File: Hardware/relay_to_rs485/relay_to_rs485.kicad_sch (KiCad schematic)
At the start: 38 parts, among them J1 Relay Inputs A to E connected, J2 RS485 Output Screw Terminal, J3 Screw_Terminal_InputGrounds, J4 Jack-DC, J5 UART OUT, Q1 IRLML6401, U1 ESP32-S3-WROOM-1, U2 MAX485E, U3 SMX1117MP-3.3

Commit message: Minor rotation of J2 labelling on schematic
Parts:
- added TP16, TP17: ~, TestPoint:TestPoint_Pad_1.5x1.5mm, symbol Connector:TestPoint_Probe
- renumbered TP1 to TP1_A1, TP2 to TP2_B1, TP3 to TP3_C1, TP4 to TP4_D1, TP5 to TP5_E1, TP6 to TP6_F1, TP7 to TP7_G1, TP8 to TP8_H1
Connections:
- net RX: now also TP17.1
- net TX: now also TP16.1
- net at U1.35 (IO42), U2.1 (RO): now also TP11.1
- net at U1.30 (IO37), U2.2 (~{RE}), U2.3 (DE): no longer TP11.1

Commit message: various edits
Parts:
- added R4, R5: 680R, Resistor_SMD:R_0805_2012Metric_Pad1.20x1.40mm_HandSolder, symbol Device:R
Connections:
- net +3V3: now also R4.1
- net A: now also R4.2
- net B: now also R5.1
- net GND: now also R5.2

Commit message: Changed decoupling resistor values from 100uF to 1uF
Too high capacitance
Also changed silkscreen for R1 to make clear terminating resistor
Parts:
- C2, C4, C7: value 100uF -> 1uF
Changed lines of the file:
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@@
 			)
 		)
-		(property "Value" "100uF"
+		(property "Value" "1uF"
 			(at 214.122 77.724 90)
 			(effects
@@
 			)
 		)
-		(property "Value" "100uF"
+		(property "Value" "1uF"
 			(at 141.732 68.834 90)
 			(effects
@@
 		)
 		(property "Value" "Jack-DC"
-			(at 19.05 29.2101 0)
+			(at 19.05 35.306 90)
 			(effects
 				(font
@@
 			)
 		)
-		(property "Value" "100uF"
+		(property "Value" "1uF"
 			(at 61.214 43.434 90)
 			(effects

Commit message: Change of DC polarity marking on PCB
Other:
- title: (none) -> Relay to RS485 Module
- moved on the sheet: R1
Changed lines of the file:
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@@
 	(generator_version "8.0")
 	(paper "A4")
+	(title_block
+		(title "Relay to RS485 Module")
+		(date "2024-09-09")
+	)
 	(junction
 		(at 60.96 35.56)
@@
 	)
 	(junction
+		(at 238.76 106.68)
+		(diameter 0)
+		(color 0 0 0 0)
+	)
+	(junction
 		(at 218.44 86.36)
 		(diameter 0)
@@
 	)
 	(junction
+		(at 238.76 101.6)
+		(diameter 0)
+		(color 0 0 0 0)
+	)
+	(junction
 		(at 251.46 101.6)
 		(diameter 0)
@@
 	(wire
 		(pts
-			(xy 232.41 101.6) (xy 245.11 101.6)
+			(xy 232.41 101.6) (xy 238.76 101.6)
 		)
 		(stroke
@@
 	(wire
 		(pts
-			(xy 232.41 106.68) (xy 250.19 106.68)
+			(xy 232.41 106.68) (xy 238.76 106.68)
 		)
 		(stroke
@@
 	(wire
 		(pts
+			(xy 238.76 106.68) (xy 250.19 106.68)
+		)
+		(stroke
+			(width 0)
+			(type default)
+		)
+	)
+	(wire
+		(pts
 			(xy 53.34 35.56) (xy 48.26 35.56)
 		)
@@
 		(pts
 			(xy 250.19 106.68) (xy 250.19 110.49)
+		)
+		(stroke
+			(width 0)
+			(type default)
+		)
+	)
+	(wire
+		(pts
+			(xy 238.76 101.6) (xy 245.11 101.6)
 		)
 		(stroke
@@
 	(symbol
 		(lib_id "Device:R_Small")
-		(at 232.41 104.14 0)
+		(at 238.76 104.14 0)
 		(unit 1)
 		(exclude_from_sim no)
@@
 		(fields_autoplaced yes)
 		(property "Reference" "R1"
-			(at 234.95 102.8699 0)
+			(at 241.3 102.8699 0)
 			(effects
 				(font
@@
 		)
 		(property "Value" "100R"
-			(at 234.95 105.4099 0)
+			(at 241.3 105.4099 0)
 			(effects
 				(font
@@
 		)
 		(property "Footprint" "Resistor_SMD:R_0805_2012Metric_Pad1.20x1.40mm_HandSolder"
-			(at 232.41 104.14 0)
+			(at 238.76 104.14 0)
 			(effects
 				(font
@@
 		)
 		(property "Datasheet" "~"
-			(at 232.41 104.14 0)
+			(at 238.76 104.14 0)
 			(effects
 				(font
@@
 		)
 		(property "Description" "Resistor, small symbol"
-			(at 232.41 104.14 0)
-			(effects
-				(font
+			(at 238.76 104.14 0)
+			(effects
+				(font

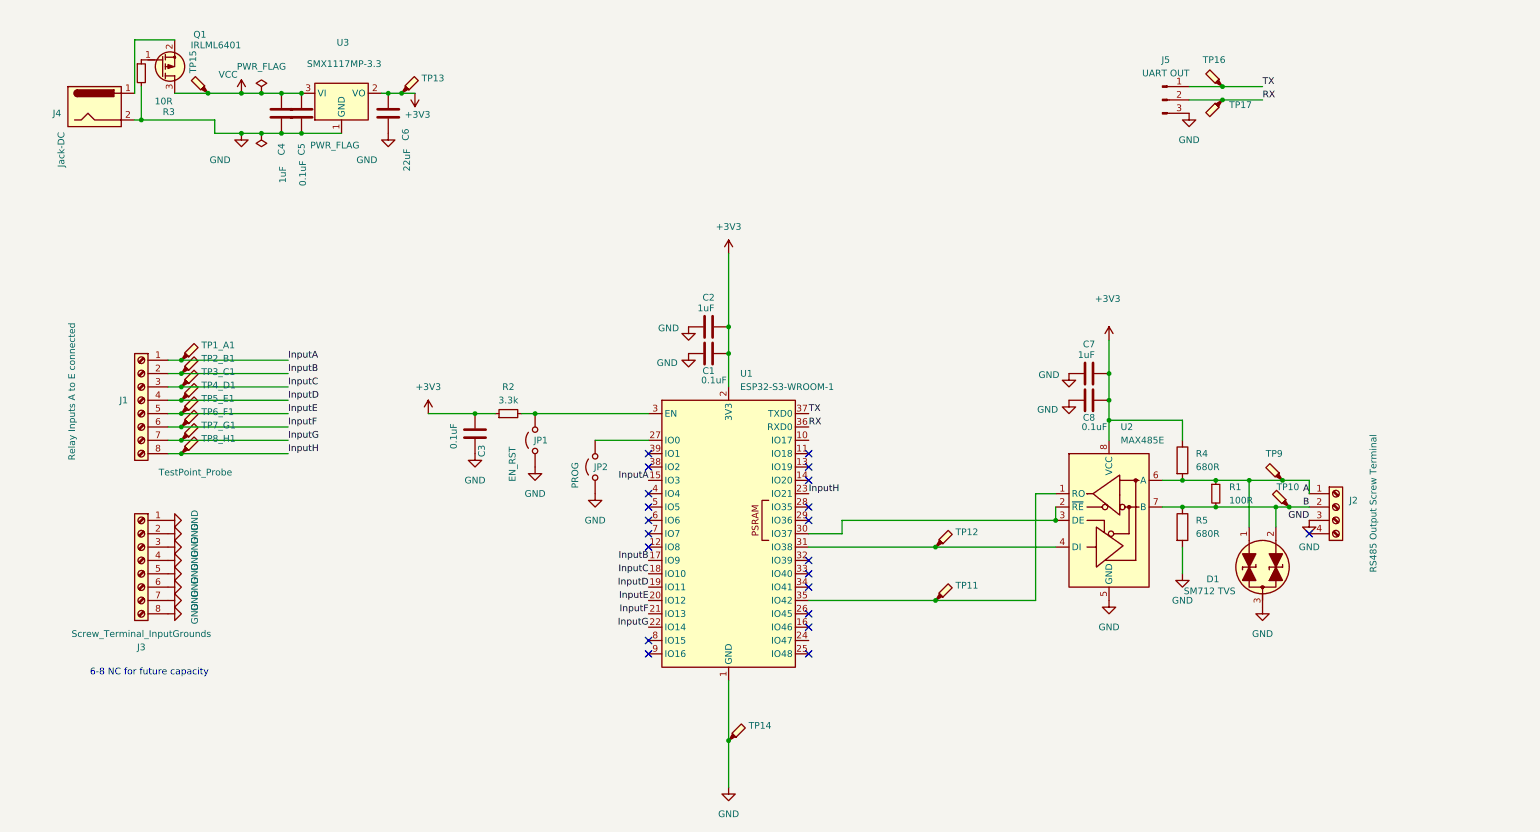
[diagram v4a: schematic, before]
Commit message: Revision B of Board (2.0.0)
Add:
1. LC filter on 3.3V input
2. Change trace widths to 20mil for 3.3V and 25mil for VCC as per Espressif documentation
3. Add-in 470R UART Tx resistors to suppress 80MHz harmonics
4. Rerouting of components around MAX3485 chip
5. Change value of R2 EN pullup resistor to 4.7k
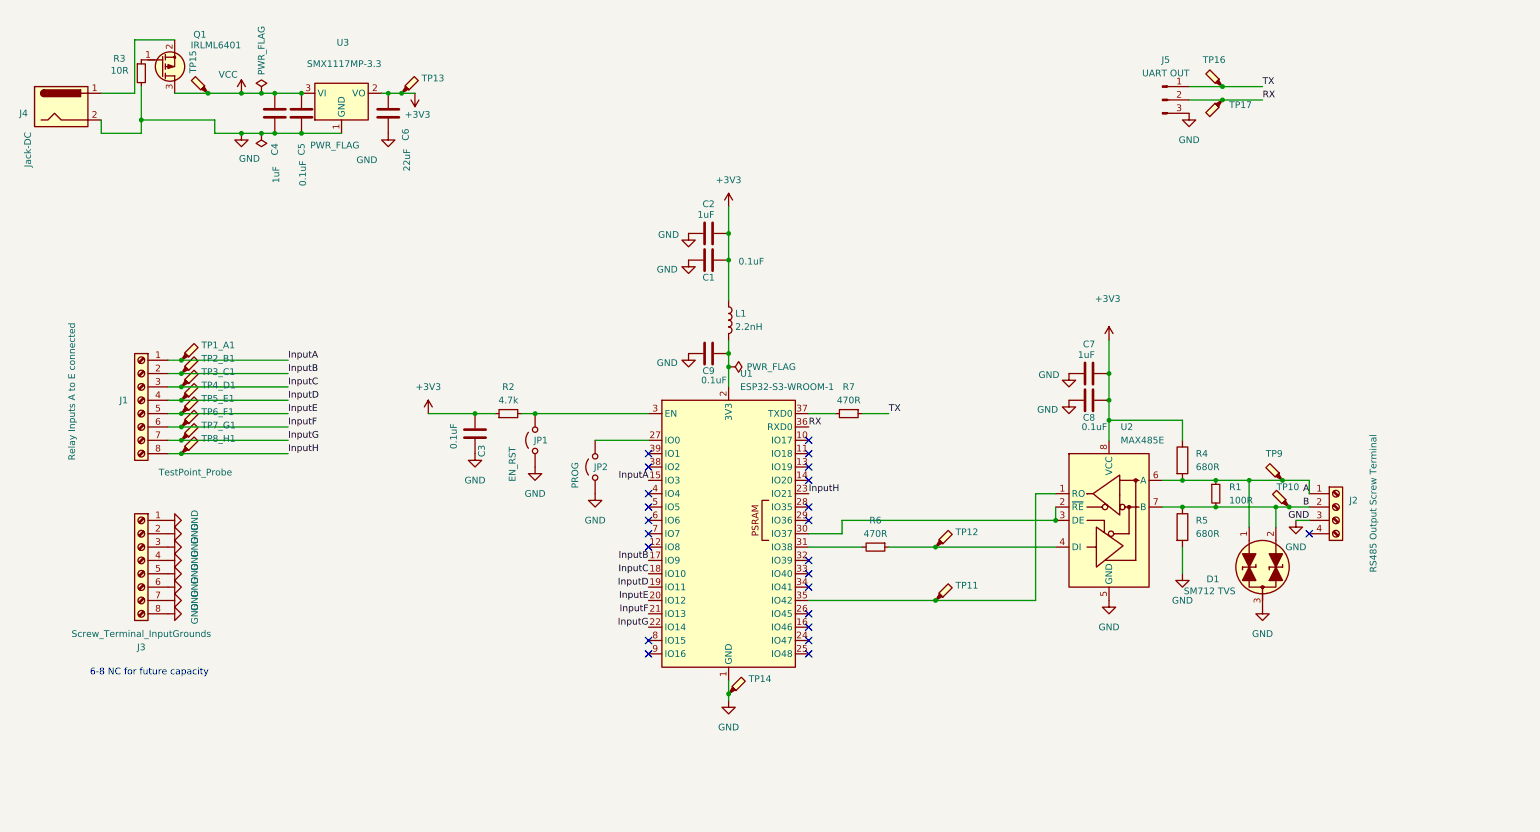
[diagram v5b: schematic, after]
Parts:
- added C9: 0.1uF, Capacitor_SMD:C_0805_2012Metric_Pad1.18x1.45mm_HandSolder, symbol Device:C
- added L1: 2.2nH, PCM_Inductor_SMD_AKL:L_0805_2012Metric_Pad1.05x1.20mm_HandSolder, symbol Device:L
- added R6, R7: 470R, Resistor_SMD:R_0805_2012Metric_Pad1.20x1.40mm_HandSolder, symbol Device:R_Small
- R2: value 3.3k -> 4.7k
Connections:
- net +3V3: now also L1.1; no longer U1.2 (3V3)
- net GND: now also C9.2
- net TX: now also R7.1; no longer U1.37 (TXD0)
- net at TP12.1, U2.4 (DI): now also R6.1; no longer U1.31 (IO38)
- new net: C9.1, L1.2, U1.2 (3V3)
- new net: R6.2, U1.31 (IO38)
- new net: R7.2, U1.37 (TXD0)
- no-connect marks 21 -> 23
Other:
- moved on the sheet: C1, C2, C4, J4, TP14

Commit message: More changes
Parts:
- added DZ1: 7.5 or 8.2, PCM_Diode_SMD_Handsoldering_AKL:D_SOD-123_Zener, symbol PCM_Diode_Zener_AKL:D_Zener_Generic
- J4: value Jack-DC -> Max 12VDC IN
- R3: value 10R -> 100R
- R4, R5: value 680R -> 330R
- renumbered TP10 to TP10_B1, TP13 to TP13_3V3, TP14 to TP14_GND1, TP15 to TP15_VCC1, TP16 to TP16_TX1, TP17 to TP17_RX1, TP9 to TP9_A1
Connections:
- net B is gone; now on net GND: D1.2 (A2), J2.2 (Pin_2), R1.2, R5.1, TP10_B1.1, U2.7 (B)
- net GND: now also DZ1.2 (A)
- net VCC: now also Q1.2 (S), DZ1.1 (K); no longer Q1.3 (D)
- net at J4.1: now also Q1.3 (D); no longer Q1.2 (S)
- net A renamed A+
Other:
- moved on the sheet: D1, R1, R3, R4, R5
